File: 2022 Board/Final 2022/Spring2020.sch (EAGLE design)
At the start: 21 parts, among them U1 TB67H401FTG(O,EL), U2 ABX00012

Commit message: Almost completely working board
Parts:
- removed CVM1: 860010674014, Test:860010674014
- added 5V1, 5V2: (no value), pinhead:PINHD-1X2
- added C1: CL05A105KP5NNNC, SnapEDA Library:CL05A105KP5NNNC
- C2: value (none) -> CL05A105KP5NNNC; device resistor:C-US025-050X050 -> SnapEDA Library:CL05A105KP5NNNC
- C3: value (none) -> UVY1H102MHD; device resistor:C-US025-050X050 -> Test2:UVY1H102MHD
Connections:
- removed net N$10: FRT_ENCODE.8
- removed net N$4: FRT_ENCODE.4
- removed net N$6: U2.PA08_S0_I2C_SDA
- removed net N$7: U2.PA09_S0_I2C_SCL
- new net FLMT: FRT_ENCODE.4, U2.PA06_AIN6/A5
- new net RLMT: FRT_ENCODE.8, U2.PA07_AIN7/A6
- net 3.3V: now also C1.1; no longer C2.1
- net 5V: now also 5V1.2, 5V2.2, C2.2; no longer C3.1
- net BKPWR: now also C3.2, PWR_IN.1, REAR_PWR.2; no longer CVM1.2, PWR_IN.2, REAR_PWR.1
- net F+: now also FRT_MTR.1; no longer FRT_MTR.2
- net F-: now also FRT_MTR.2; no longer FRT_MTR.1
- net FRT_PWM: now also U2.PB11_TCC0-W5/~5
- net GND: now also 5V1.1, 5V2.1, C1.2, C2.1, C3.1, PWR_IN.2, REAR-MOTOR.4, REAR_PWR.1; no longer C2.2, C3.2, CVM1.1, PWR_IN.1, REAR-MOTOR.1, REAR_PWR.2
- net IMU-CS: now also IMU.4, U2.PA08_S0_I2C_SDA; no longer IMU.2, U2.PA21_TCC0-W7
- net I_1: now also U2.PB10_TCC0-W4/~4
- net I_2: now also U2.PA11_TCC0-W3/~3
- net QUAD-A: now also U2.PA21_TCC0-W7
- net QUAD-B: now also U2.PA20_TCC0-W6
- net REAR-PWM: now also U2.PA22_TC4-W0/0; no longer U2.PA11_TCC0-W3/~3
- net REAR-PWMOUT: now also REAR-MOTOR.1; no longer REAR-MOTOR.2
- net REAR-TIMER: now also REAR-MOTOR.3; no longer REAR-MOTOR.4
- net REAR-TIMER-IN: now also U2.PA09_S0_I2C_SCL
- net REVERSE: now also REAR-MOTOR.2; no longer REAR-MOTOR.3
- net SCK: now also IMU.2; no longer IMU.4
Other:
- moved on the sheet: C2, PWR_IN, REAR_PWR

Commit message: Just a few random edits
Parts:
- removed C3: UVY1H102MHD, Test2:UVY1H102MHD
- added CMV1: UVY1H102MHD, Test2:UVY1H102MHD
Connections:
- net BKPWR: now also CMV1.2; no longer C3.2
- net FLMT: no longer U2.PA06_AIN6/A5
- net FRT_PWM: now also U2.PA22_TC4-W0/0; no longer U2.PB11_TCC0-W5/~5
- net GND: now also CMV1.1; no longer C3.1
- net I_1: now also U2.PA10_TCC0-W2/~2; no longer U2.PB10_TCC0-W4/~4
- net I_2: now also U2.PA23_TC4-W1/1; no longer U2.PA11_TCC0-W3/~3
- net QUAD-A: now also U2.PA20_TCC0-W6; no longer U2.PA21_TCC0-W7
- net QUAD-B: now also U2.PA21_TCC0-W7; no longer U2.PA20_TCC0-W6
- net REAR-PWM: now also U2.PA11_TCC0-W3/~3; no longer U2.PA22_TC4-W0/0
- net REAR-TIMER-IN: now also U2.PB10_TCC0-W4/~4; no longer U2.PA09_S0_I2C_SCL, U2.PA23_TC4-W1/1
- net REVERSE_IN: now also U2.PB11_TCC0-W5/~5; no longer U2.PA10_TCC0-W2/~2
- net RLMT: no longer U2.PA07_AIN7/A6
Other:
- moved on the sheet: 5V1, 5V2, COSC, CVM2, FRT_ENCODE, FRT_MTR, IMU, PS1, PWR_IN, RC, REAR_PWR, ROSC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

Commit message: DONE!
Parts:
- removed U$2, U$7: IL-712, Spring2016Optoisolator:IL-712
- added ISO_1, ISO_2: π121U31, SnapEDA Library:π121U31
- FRT_ENCODE: device Test:3220-10-0100-00 -> SnapEDA Library:3220-10-0100-00
- FRT_MTR, PWR_IN, REAR_PWR: value 1792863 -> 2060-452_998-404; device Test:1792863 -> 2060-452_998-404:2060-452_998-404
- ROSC: value RC0100JR-075K1L -> (none); device SnapEDA Library:RC0100JR-075K1L -> rcl:R-US_R0402
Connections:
- net 3.3V: now also ISO_1.1, ISO_2.1; no longer U$2.VDD1, U$7.VDD1
- net 5V: now also ISO_1.8, ISO_2.8; no longer U$2.VDD2, U$7.VDD2
- net BKPWR: now also PWR_IN.3, REAR_PWR.4
- net F+: now also FRT_MTR.2, FRT_MTR.4; no longer FRT_MTR.1
- net F-: now also FRT_MTR.1, FRT_MTR.3; no longer FRT_MTR.2
- net GND: now also ISO_1.4, ISO_1.5, ISO_2.4, ISO_2.5, PWR_IN.4, REAR_PWR.3; no longer U$2.GND1, U$2.GND2, U$7.GND1, U$7.GND2
- net REAR-PWM: now also ISO_2.2; no longer U$7.IN1
- net REAR-PWM-5V: now also ISO_2.7; no longer U$7.OUT1
- net REAR-TIMER: now also ISO_1.6; no longer U$2.IN2
- net REAR-TIMER-IN: now also ISO_1.3; no longer U$2.OUT2
- net REVERSE: now also ISO_1.7; no longer U$2.OUT1
- net REVERSE_IN: now also ISO_1.2; no longer U$2.IN1
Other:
- note removed: "Isolator 2"
- moved on the sheet: C1, C2

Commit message: Almost done
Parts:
- added RRS1: RLP73K3AR22FTDF, SnapEDA Library:RLP73K3AR22FTDF
- RRS: value CSRL3-0R15F8 -> RLP73K3AR22FTDF; device Test:CSRL3-0R15F8 -> SnapEDA Library:RLP73K3AR22FTDF
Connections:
- net BKPWR: now also RRS1.1
- net RS: now also RRS1.2
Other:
- moved on the sheet: CMV1, CVM2

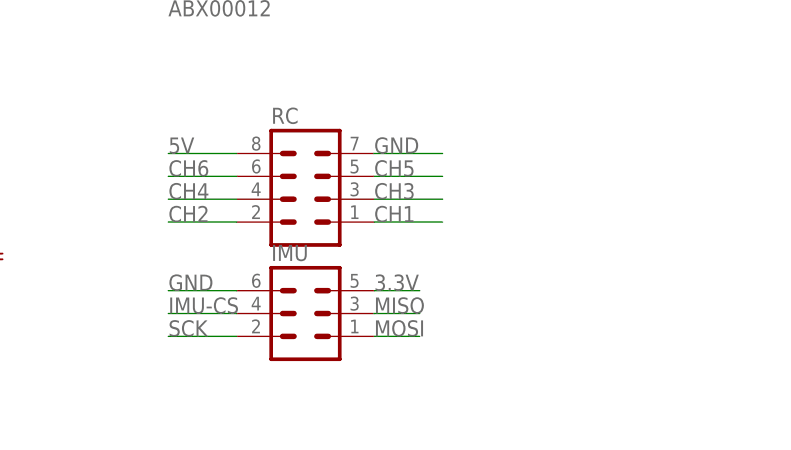
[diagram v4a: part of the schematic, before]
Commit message: Changed IMU voltage
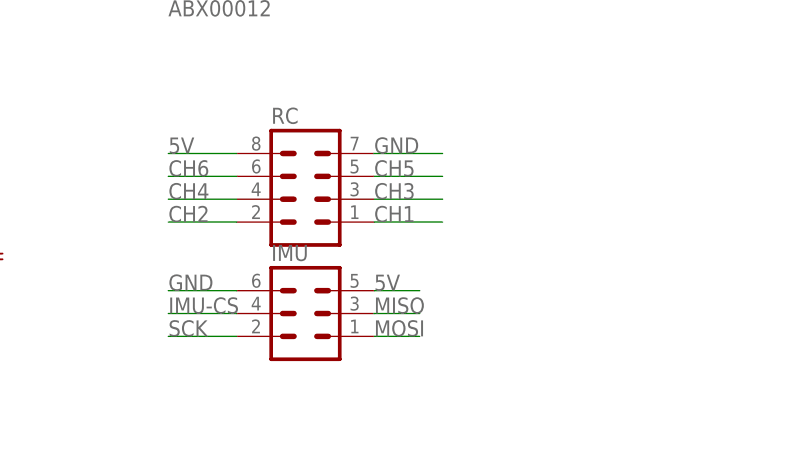
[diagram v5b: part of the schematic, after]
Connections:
- net 3.3V: no longer IMU.5
- net 5V: now also IMU.5
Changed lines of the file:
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@@
-</segment>
-<segment>
-<pinref part="IMU" gate="1" pin="5"/>
-<wire x1="256.54" y1="35.56" x2="261.62" y2="35.56" width="0.1524" layer="91"/>
-<label x="256.54" y="35.56" size="1.778" layer="95"/>
 </segment>
 <segment>
@@
 <label x="243.84" y="124.46" size="1.778" layer="95"/>
 </segment>
-</net>
+<segment>
+<pinref part="IMU" gate="1" pin="5"/>
+<wire x1="256.54" y1="35.56" x2="261.62" y2="35.56" width="0.1524" layer="91"/>
+<label x="256.54" y="35.56" size="1.778" layer="95"/>
+</segment>
+</net>
